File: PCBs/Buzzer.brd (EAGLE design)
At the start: 15 x 39.9 mm, 3 parts

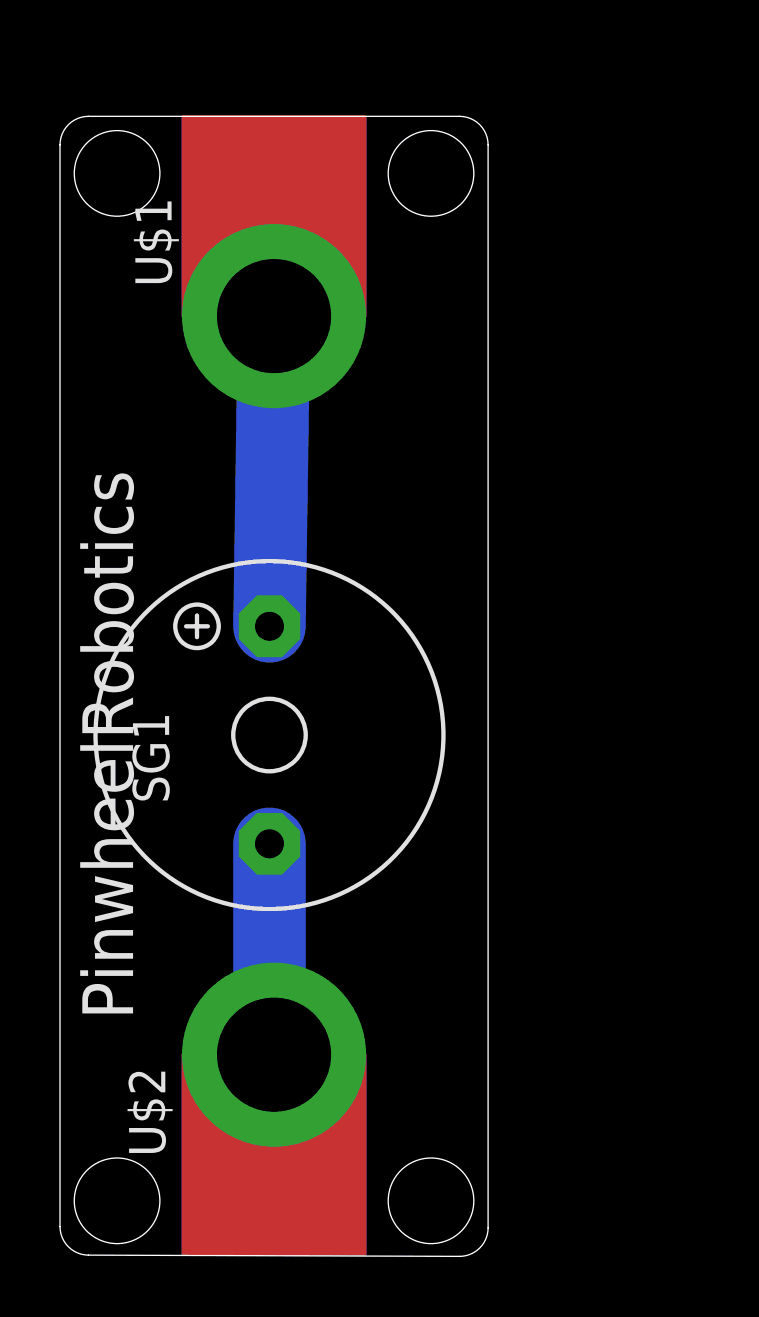
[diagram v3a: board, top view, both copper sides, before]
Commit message: Dimension added
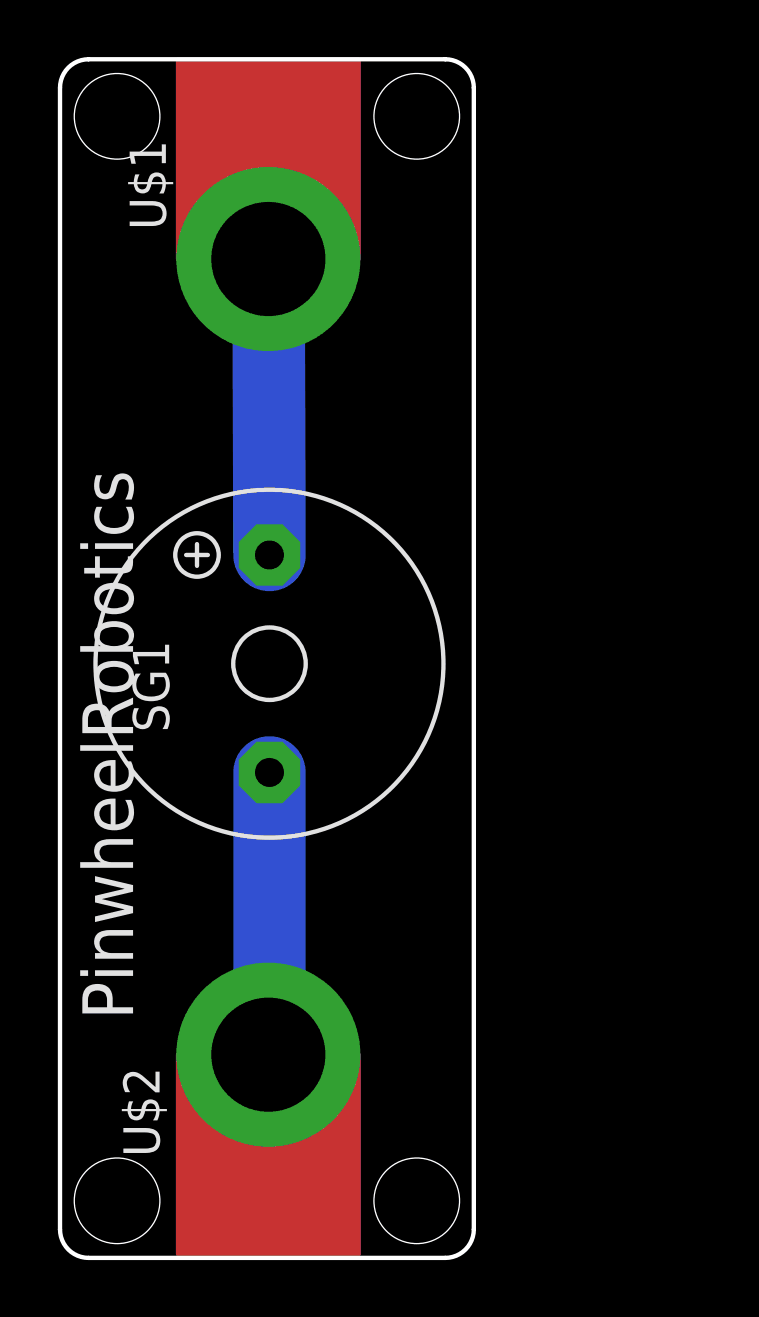
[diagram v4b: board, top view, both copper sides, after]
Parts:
- moved SG1 2.50 mm to (7.34, 20.8)
- moved U$1 2.01 mm to (7.30, 35.0)
- moved U$2 0.20 mm to (7.30, 7.12)
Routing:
- net N$2: track 8.21 -> 10.7 mm
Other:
- board size 15 x 39.9 mm -> 14.5 x 42 mm
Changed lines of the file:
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@@
 <board>
 <plain>
-<wire x1="0.996665625" y1="0.096678125" x2="13.996665625" y2="0.05334375" width="0" layer="20"/>
-<wire x1="13.996665625" y1="0.05334375" x2="15" y2="1.0533375" width="0" layer="20" curve="90.173081"/>
-<wire x1="15" y1="1.0533375" x2="15" y2="39" width="0" layer="20"/>
-<wire x1="15" y1="39" x2="14" y2="40" width="0" layer="20" curve="90"/>
-<wire x1="14" y1="40" x2="1" y2="40" width="0" layer="20"/>
-<wire x1="1" y1="40" x2="0" y2="39" width="0" layer="20" curve="90"/>
-<wire x1="0" y1="39" x2="0" y2="1.096671875" width="0" layer="20"/>
-<wire x1="0" y1="1.096671875" x2="0.996665625" y2="0.096678125" width="0" layer="20" curve="89.808954"/>
-<hole x="2" y="38" drill="3"/>
-<hole x="13" y="38" drill="3"/>
+<hole x="2" y="40" drill="3"/>
+<hole x="12.5" y="40" drill="3"/>
 <hole x="2" y="2" drill="3"/>
-<hole x="13" y="2" drill="3"/>
+<hole x="12.5" y="2" drill="3"/>
 <text x="13.54" y="26.05" size="1.778" layer="22" rot="MR270">care@pinwheel</text>
 <text x="2.56" y="8.35" size="1.778" layer="21" rot="R90">PinwheelRobotics</text>
+<wire x1="1" y1="0" x2="13.5" y2="0" width="0.1524" layer="20"/>
+<wire x1="13.5" y1="0" x2="14.5" y2="1" width="0.1524" layer="20" curve="90"/>
+<wire x1="14.5" y1="1" x2="14.5" y2="41" width="0.1524" layer="20"/>
+<wire x1="14.5" y1="41" x2="13.5" y2="42" width="0.1524" layer="20" curve="90"/>
+<wire x1="13.5" y1="42" x2="1" y2="42" width="0.1524" layer="20"/>
+<wire x1="1" y1="42" x2="0" y2="41" width="0.1524" layer="20" curve="90"/>
+<wire x1="0" y1="41" x2="0" y2="1" width="0.1524" layer="20"/>
+<wire x1="0" y1="1" x2="1" y2="0" width="0.1524" layer="20" curve="90"/>
 </plain>
 <attributes>
@@
 </autorouter>
 <elements>
-<element name="SG1" library="buzzer" library_urn="urn:adsk.eagle:library:113" package="F/TMB" package3d_urn="urn:adsk.eagle:package:5260/1" value="F/TMB" x="7.34" y="18.32" smashed="yes" rot="R90">
-<attribute name="MF" value="" x="13.69" y="38.64" size="1.778" layer="27" rot="R90" display="off"/>
-<attribute name="MPN" value="" x="13.69" y="38.64" size="1.778" layer="27" rot="R90" display="off"/>
-<attribute name="NAME" x="3.825" y="15.922" size="1.27" layer="25" ratio="10" rot="R90"/>
-<attribute name="OC_FARNELL" value="unknown" x="13.69" y="38.64" size="1.778" layer="27" rot="R90" display="off"/>
-<attribute name="OC_NEWARK" value="unknown" x="13.69" y="38.64" size="1.778" layer="27" rot="R90" display="off"/>
-<attribute name="POPULARITY" value="1" x="13.69" y="38.64" size="1.778" layer="27" rot="R90" display="off"/>
-<attribute name="VALUE" x="11.15" y="14.51" size="1.27" layer="27" ratio="10" rot="R90"/>
+<element name="SG1" library="buzzer" library_urn="urn:adsk.eagle:library:113" package="F/TMB" package3d_urn="urn:adsk.eagle:package:5260/1" value="F/TMB" x="7.34" y="20.82" smashed="yes" rot="R90">
+<attribute name="MF" value="" x="13.69" y="41.14" size="1.778" layer="27" rot="R90" display="off"/>
+<attribute name="MPN" value="" x="13.69" y="41.14" size="1.778" layer="27" rot="R90" display="off"/>
+<attribute name="NAME" x="3.825" y="18.422" size="1.27" layer="25" ratio="10" rot="R90"/>
+<attribute name="OC_FARNELL" value="unknown" x="13.69" y="41.14" size="1.778" layer="27" rot="R90" display="off"/>
+<attribute name="OC_NEWARK" value="unknown" x="13.69" y="41.14" size="1.778" layer="27" rot="R90" display="off"/>
+<attribute name="POPULARITY" value="1" x="13.69" y="41.14" size="1.778" layer="27" rot="R90" display="off"/>
+<attribute name="VALUE" x="11.15" y="17.01" size="1.27" layer="27" ratio="10" rot="R90"/>
 </element>
-<element name="U$1" library="microbit" package="MICROBIT_PAD" value="MICROBIT_PAD" x="7.5" y="33" smashed="yes" rot="R180">
-<attribute name="NAME" x="3.91" y="34.02" size="1.27" layer="21" rot="R90"/>
+<element name="U$1" library="microbit" package="MICROBIT_PAD" value="MICROBIT_PAD" x="7.3" y="35" smashed="yes" rot="R180">
+<attribute name="NAME" x="3.71" y="36.02" size="1.27" layer="21" rot="R90"/>
 </element>
-<element name="U$2" library="microbit" package="MICROBIT_PAD" value="MICROBIT_PAD" x="7.5" y="7.12" smashed="yes">
-<attribute name="NAME" x="3.69" y="3.54" size="1.27" layer="21" rot="R90"/>
+<element name="U$2" library="microbit" package="MICROBIT_PAD" value="MICROBIT_PAD" x="7.3" y="7.12" smashed="yes">
+<attribute name="NAME" x="3.49" y="3.54" size="1.27" layer="21" rot="R90"/>
 </element>
 </elements>
@@
 <contactref element="SG1" pad="+"/>
 <contactref element="U$1" pad="PAD"/>
-<wire x1="7.34" y1="22.13" x2="7.5" y2="33" width="2.54" layer="16"/>
+<wire x1="7.34" y1="24.63" x2="7.30779375" y2="34.99220625" width="2.54" layer="16"/>
+<wire x1="7.30779375" y1="34.99220625" x2="7.3" y2="35" width="2.54" layer="16"/>
 </signal>
 <signal name="N$2">
@@
 <contactref element="U$2" pad="PAD"/>
 <wire x1="6.917034375" y1="4.382634375" x2="6.6304" y2="4.096" width="0.1524" layer="16"/>
-<wire x1="7.34" y1="14.51" x2="7.34" y2="7.36" width="2.54" layer="16"/>
+<wire x1="7.34" y1="17.01" x2="7.34" y2="7.36" width="2.54" layer="16"/>
 <wire x1="7.34" y1="7.36" x2="7.8" y2="6.9" width="2.54" layer="16"/>
-<wire x1="7.8" y1="6.9" x2="7.5" y2="7.12" width="0" layer="19" extent="16-16"/>
+<wire x1="7.8" y1="6.9" x2="7.3" y2="7.12" width="0" layer="19" extent="16-16"/>
 <wire x1="6.917034375" y1="4.382634375" x2="7.8" y2="6.9" width="0" layer="19" extent="16-16"/>
 </signal>
